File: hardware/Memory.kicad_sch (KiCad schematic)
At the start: 13 parts, among them J15 Micro_SD_Card_Det_Hirose_DM3AT, U20 AT45DB641E-SHN-T

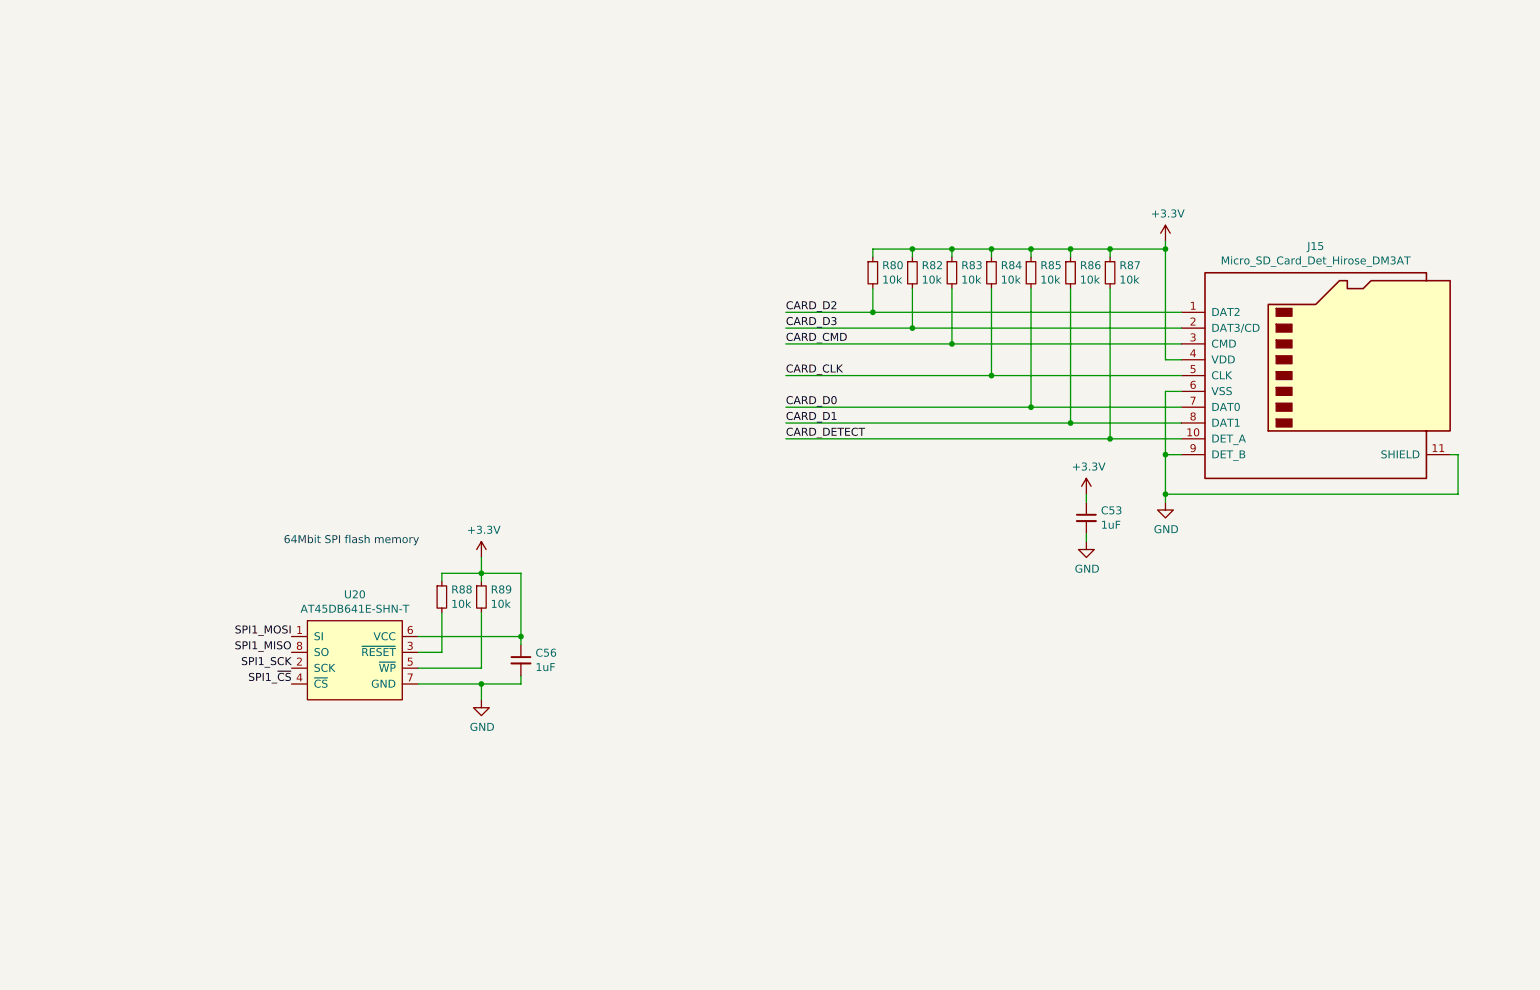
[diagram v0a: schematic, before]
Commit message: finished remaking whole schematic
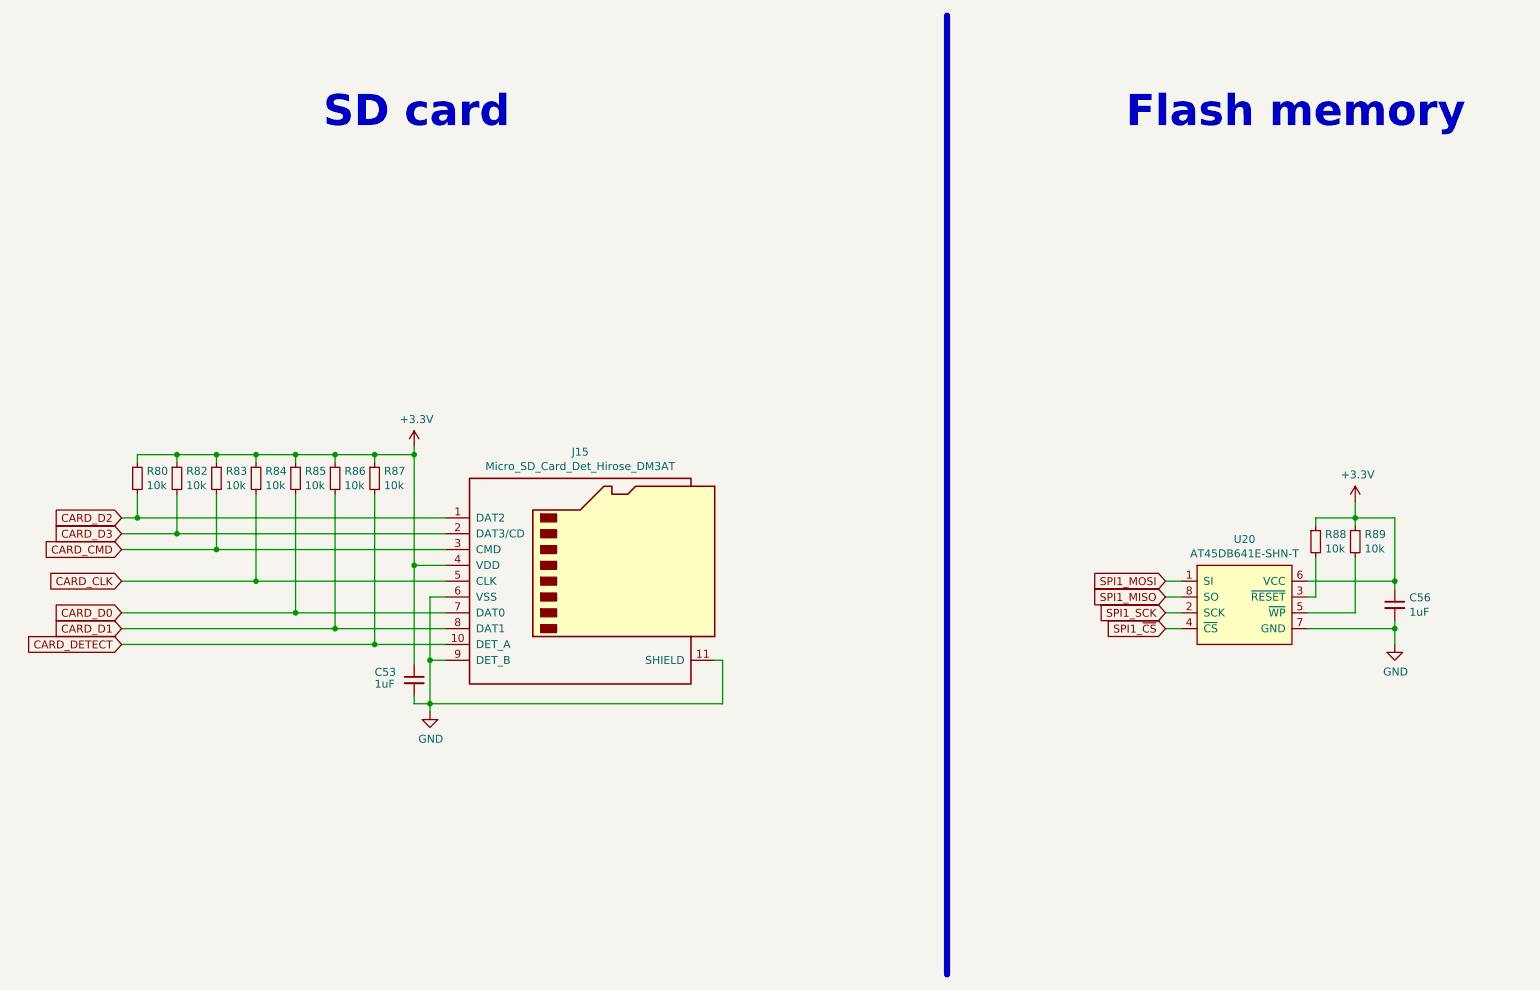
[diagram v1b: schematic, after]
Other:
- note added: "Flash memory"
- note added: "SD card"
- note removed: "64Mbit SPI flash memory"
- moved on the sheet: C53, C56, J15, R80, R82, R83, R84, R85, R86, R87, R88, R89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

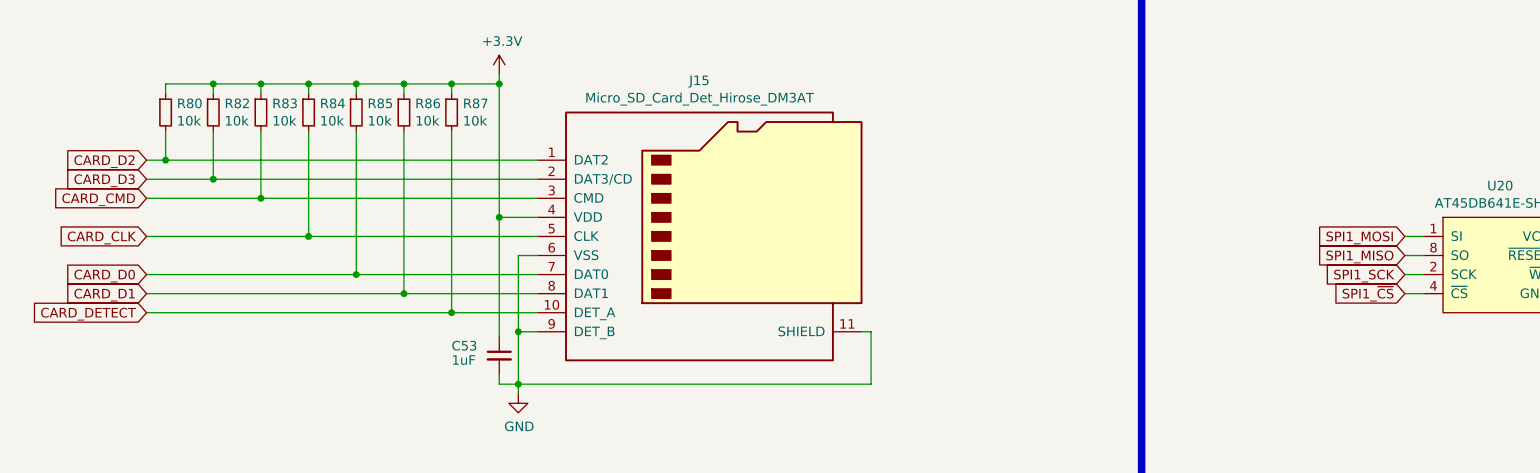
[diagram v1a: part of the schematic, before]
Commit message: Schematic readability update
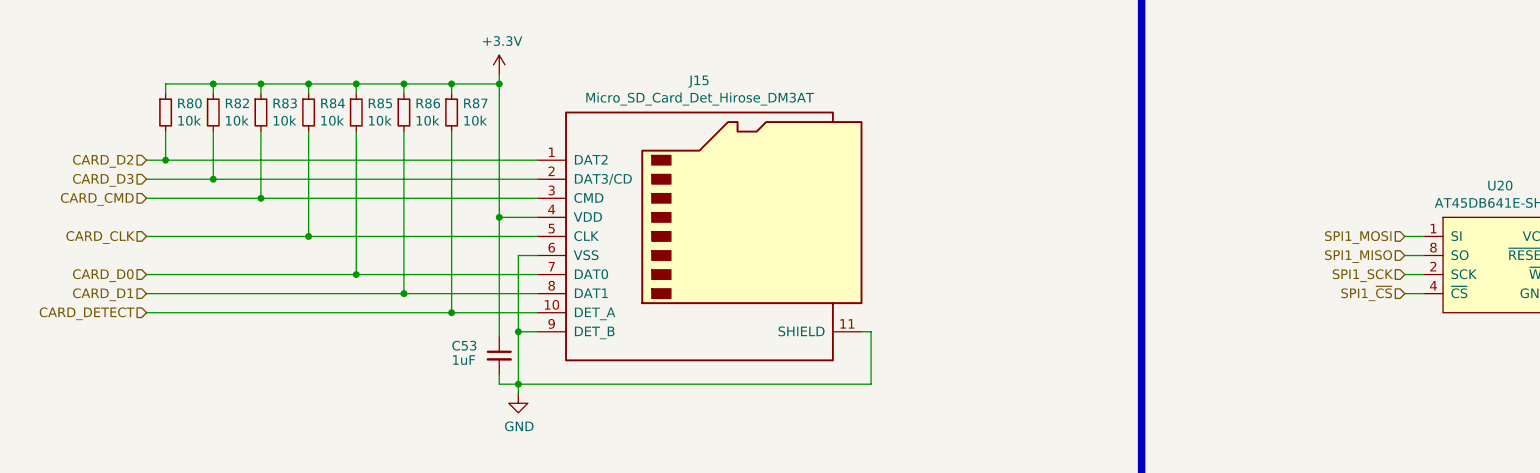
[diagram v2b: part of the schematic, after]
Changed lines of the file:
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@@
     (effects (font (size 5 5) (thickness 1) bold) (justify left bottom))
   )
-  (global_label "CARD_CLK" (shape input) (at 44.45 102.87 180) (fields_autoplaced)
+  (hierarchical_label "CARD_D1" (shape input) (at 44.45 110.49 180)
     (effects (font (size 1.27 1.27)) (justify right))
-    (property "Intersheet References" "${INTERSHEET_REFS}" (id 0) (at 32.6915 102.7906 0)
-      (effects (font (size 1.27 1.27)) (justify right) hide)
-    )
   )
-  (global_label "CARD_D0" (shape input) (at 44.45 107.95 180) (fields_autoplaced)
+  (hierarchical_label "CARD_CMD" (shape input) (at 44.45 97.79 180)
     (effects (font (size 1.27 1.27)) (justify right))
-    (property "Intersheet References" "${INTERSHEET_REFS}" (id 0) (at 33.7801 107.8706 0)
-      (effects (font (size 1.27 1.27)) (justify right) hide)
-    )
   )
-  (global_label "SPI1_MISO" (shape input) (at 212.09 105.41 180) (fields_autoplaced)
+  (hierarchical_label "CARD_D0" (shape input) (at 44.45 107.95 180)
     (effects (font (size 1.27 1.27)) (justify right))
-    (property "Intersheet References" "${INTERSHEET_REFS}" (id 0) (at 199.9082 105.3306 0)
-      (effects (font (size 1.27 1.27)) (justify right) hide)
-    )
   )
-  (global_label "SPI1_SCK" (shape input) (at 212.09 107.95 180) (fields_autoplaced)
+  (hierarchical_label "CARD_DETECT" (shape input) (at 44.45 113.03 180)
     (effects (font (size 1.27 1.27)) (justify right))
-    (property "Intersheet References" "${INTERSHEET_REFS}" (id 0) (at 200.7548 107.8706 0)
-      (effects (font (size 1.27 1.27)) (justify right) hide)
-    )
   )
-  (global_label "SPI1_MOSI" (shape input) (at 212.09 102.87 180) (fields_autoplaced)
+  (hierarchical_label "SPI1_MISO" (shape input) (at 212.09 105.41 180)
     (effects (font (size 1.27 1.27)) (justify right))
-    (property "Intersheet References" "${INTERSHEET_REFS}" (id 0) (at 199.9082 102.7906 0)
-      (effects (font (size 1.27 1.27)) (justify right) hide)
-    )
   )
-  (global_label "SPI1_~{CS}" (shape input) (at 212.09 110.49 180) (fields_autoplaced)
+  (hierarchical_label "CARD_D2" (shape input) (at 44.45 92.71 180)
     (effects (font (size 1.27 1.27)) (justify right))
-    (property "Intersheet References" "${INTERSHEET_REFS}" (id 0) (at 202.0248 110.4106 0)
-      (effects (font (size 1.27 1.27)) (justify right) hide)
-    )
   )
-  (global_label "CARD_D1" (shape input) (at 44.45 110.49 180) (fields_autoplaced)
+  (hierarchical_label "CARD_CLK" (shape input) (at 44.45 102.87 180)
     (effects (font (size 1.27 1.27)) (justify right))
-    (property "Intersheet References" "${INTERSHEET_REFS}" (id 0) (at 33.7801 110.4106 0)
-      (effects (font (size 1.27 1.27)) (justify right) hide)
-    )
   )
-  (global_label "CARD_D2" (shape input) (at 44.45 92.71 180) (fields_autoplaced)
+  (hierarchical_label "SPI1_MOSI" (shape input) (at 212.09 102.87 180)
     (effects (font (size 1.27 1.27)) (justify right))
-    (property "Intersheet References" "${INTERSHEET_REFS}" (id 0) (at 33.7801 92.6306 0)
-      (effects (font (size 1.27 1.27)) (justify right) hide)
-    )
   )
-  (global_label "CARD_DETECT" (shape input) (at 44.45 113.03 180) (fields_autoplaced)
+  (hierarchical_label "SPI1_~{CS}" (shape input) (at 212.09 110.49 180)
     (effects (font (size 1.27 1.27)) (justify right))
-    (property "Intersheet References" "${INTERSHEET_REFS}" (id 0) (at 29.4863 112.9506 0)
-      (effects (font (size 1.27 1.27)) (justify right) hide)
-    )
   )
-  (global_label "CARD_D3" (shape input) (at 44.45 95.25 180) (fields_autoplaced)
+  (hierarchical_label "CARD_D3" (shape input) (at 44.45 95.25 180)
     (effects (font (size 1.27 1.27)) (justify right))
-    (property "Intersheet References" "${INTERSHEET_REFS}" (id 0) (at 33.7801 95.1706 0)
-      (effects (font (size 1.27 1.27)) (justify right) hide)
-    )
   )
-  (global_label "CARD_CMD" (shape input) (at 44.45 97.79 180) (fields_autoplaced)
+  (hierarchical_label "SPI1_SCK" (shape input) (at 212.09 107.95 180)
     (effects (font (size 1.27 1.27)) (justify right))
-    (property "Intersheet References" "${INTERSHEET_REFS}" (id 0) (at 32.2682 97.7106 0)
-      (effects (font (size 1.27 1.27)) (justify right) hide)
-    )
   )
   (symbol (lib_id "Device:R_Small") (at 85.09 86.36 0) (unit 1)

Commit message: schematic override, just cuz
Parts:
- removed C56: 1uF, Capacitor_SMD:C_0603_1608Metric, symbol Device:C_Small
- removed R88, R89: 10k, Resistor_SMD:R_0603_1608Metric, symbol Device:R_Small
- removed U20: AT45DB641E-SHN-T, Package_SO:SOIC-8_5.23x5.23mm_P1.27mm, symbol PUTM_EV_BMS_library:AT45DB641E-SHN-T
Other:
- note removed: "Flash memory"

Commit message: remake in progress
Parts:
- removed R80, R86: 10k, Resistor_SMD:R_0603_1608Metric, symbol Device:R_Small
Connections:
- net CARD_CLK renamed CLK
- net CARD_CMD renamed MOSI
- net CARD_D0 renamed MISO
- net CARD_D1: no longer names the net of J15.8 (DAT1)
- net CARD_D2: no longer names the net of J15.1 (DAT2)
- net CARD_D3 renamed ~{CS}
- net CARD_DETECT renamed DET
- no-connect marks 0 -> 2
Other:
- moved on the sheet: C53, R82, R83, R84, R85, R87
